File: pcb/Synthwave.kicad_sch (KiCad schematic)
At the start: 61 parts, among them J1 Conn_01x01_Pin, J2 Conn_01x01_Pin, P1 MINI-360, P2 MINI-360, Q1 TIP120, Q10 TIP120, Q2 TIP120, Q3 TIP120, Q4 TIP120, Q5 TIP120, Q6 TIP120, Q7 TIP120, Q8 TIP120, Q9 TIP120, U1 Heltec_HTIT-WB32, U2 L9110

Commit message: Many small updates
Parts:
- added J3: ADC1, Connector_PinSocket_2.54mm:PinSocket_1x03_P2.54mm_Vertical, symbol Connector:Conn_01x03_Socket
- added J4: ADC2, Connector_PinSocket_2.54mm:PinSocket_1x03_P2.54mm_Vertical, symbol Connector:Conn_01x03_Socket
- added J5: ADC3, Connector_PinSocket_2.54mm:PinSocket_1x03_P2.54mm_Vertical, symbol Connector:Conn_01x03_Socket
- added J6: ADC4, Connector_PinSocket_2.54mm:PinSocket_1x03_P2.54mm_Vertical, symbol Connector:Conn_01x03_Socket
- U1: value Heltec_HTIT-WB32 -> Heltec_HTIT-WB32v3
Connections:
- net at R18.1, R8.2: now also U1.2 (34); no longer U1.12
- net at R16.1, R6.2: now also U1.21 (46); no longer U1.17
- net at R14.1, R4.2: now also U1.3 (47); no longer U1.33
- net at R10.2, R20.1: now also U1.19 (42); no longer U1.23
- net at R1.2, R11.1: now also U1.32 (7_ADC); no longer U1.14
- net at U1.1 (48): now also R15.1, R5.2
- net at R17.1, R7.2: now also U1.34 (5_ADC); no longer U1.13
- net at U1.15 (33): now also R13.1, R3.2
- net at U1.18 (40): now also U2.6 (IA)
- net at R19.1, R9.2: now also U1.22 (45); no longer U1.2
- net at P2.3 (OUT+): now also U1.9 (5V), J3.2 (Pin_2), J4.2 (Pin_2), J5.2 (Pin_2), J6.2 (Pin_2); no longer U1.20 (5V)
- net at R12.1, R2.2: now also U1.35 (6_ADC); no longer U1.27
- net at P2.2 (OUT-), U2.5 (GND), U2.8 (GND): now also U1.8 (GND), J3.3 (PIN_3), J4.3 (PIN_3), J5.3 (PIN_3), J6.3 (PIN_3); no longer U1.28 (GND)
- net at U2.7 (IB): now also U1.23 (41); no longer U1.34
- net at U1.36 (VBAT_1_ADC): now also J3.1 (Pin_1)
- net at U1.37 (2_ADC): now also J4.1 (Pin_1)
- net at U1.38 (3_ADC): now also J5.1 (Pin_1)
- net at U1.39 (4_ADC): now also J6.1 (Pin_1)
- now unconnected: U1.25 (25_DAC)
- no-connect marks 23 -> 1
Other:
- moved on the sheet: U1

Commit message: Update and upgrades
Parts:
- added J7, J8: RX, Connector_PinSocket_2.54mm:PinSocket_1x02_P2.54mm_Vertical, symbol Connector:Conn_01x02_Socket
- renumbered DC_OUT1 to PUMP1, DC_OUT2 to PUMP2, DC_OUT9 to REL1, DC_OUT10 to REL2, DC_OUT7 to VAC1, DC_OUT8 to VAC2, DC_OUT3 to VALVE1, DC_OUT4 to VALVE2, DC_OUT5 to VALVE3, DC_OUT6 to VALVE4
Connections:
- net at J3.2 (Pin_2), J4.2 (Pin_2), J5.2 (Pin_2)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: now also J8.2 (Pin_2)
- net at J3.3 (PIN_3), J4.3 (PIN_3), J5.3 (PIN_3)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: now also J8.1 (Pin_1)
- net at U1.12 (43_TX): now also J7.1 (Pin_1)
- net at U1.13 (44_RX): now also J7.2 (Pin_2)
- no-connect marks 1 -> 17
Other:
- note removed: "Pump_1"
- note removed: "Pump_2"
- note removed: "Release_1"
- note removed: "Release_2"
- note removed: "Vacuum_1"
- note removed: "Vacuum_2"
- note removed: "Valve_1"
- note removed: "Valve_2"
- note removed: "Valve_3"
- note removed: "Valve_4"
- moved on the sheet: J6

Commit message: updates
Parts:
- removed J1, J2: Conn_01x01_Pin, Connector_PinSocket_2.54mm:PinSocket_1x01_P2.54mm_Vertical, symbol Connector:Conn_01x01_Pin
- removed P2: MINI-360, Custom Footprints:MINI-360, symbol 74xGxx:MINI-360
- added J1: Barrel_Jack_Switch, Connector_BarrelJack:BarrelJack_Horizontal, symbol Connector:Barrel_Jack_Switch
- added J10: GPIO39, Connector_PinSocket_2.54mm:PinSocket_1x02_P2.54mm_Vertical, symbol Connector:Conn_01x02_Socket
- added J9: GPIO26, Connector_PinSocket_2.54mm:PinSocket_1x02_P2.54mm_Vertical, symbol Connector:Conn_01x02_Socket
- added NT1: NetTie_2, NetTie:NetTie-2_THT_Pad1.0mm, symbol Device:NetTie_2
- added U3: L7805, Package_TO_SOT_THT:TO-220-3_Vertical, symbol Regulator_Linear:L7805
- J7: value RX -> TX
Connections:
- net +15V: now also J1.1, U3.1 (IN)
- net GND: now also U2.5 (GND), U2.8 (GND), J1.2, NT1.2; no longer R11.2, R12.2, R13.2, R14.2, R15.2, R16.2, R17.2, R18.2, R19.2, R20.2
- net +5V: now reaches J3.2 (Pin_2), J4.2 (Pin_2), J5.2 (Pin_2), J6.2 (Pin_2), J8.2 (Pin_2), U1.9 (5V)
- net +5V: now also U3.3 (OUT)
- net GND1: now reaches J3.3 (PIN_3), J4.3 (PIN_3), J5.3 (PIN_3), J6.3 (PIN_3), J8.1 (Pin_1), U1.8 (GND)
- net GND1: now also R11.2, R12.2, R13.2, R14.2, R15.2, R16.2, R17.2, R18.2, R19.2, R20.2, J10.2 (Pin_2), J9.2 (Pin_2), NT1.1, U3.2 (GND); no longer U2.5 (GND), U2.8 (GND)
- net at U1.10 (26): now also J9.1 (Pin_1)
- net at U1.5 (39): now also J10.1 (Pin_1)
- no-connect marks 17 -> 16
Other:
- note added: "ADC breakouts for pH meters"
- note added: "GPIO breakouts for float switches"
- note added: "TX/RX breakouts for CO2 Sensor"
- note removed: "(Set to +5v)"
- moved on the sheet: D1, D10, D2, D3, D4, D5, D6, D7, D8, D9, E2, H1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

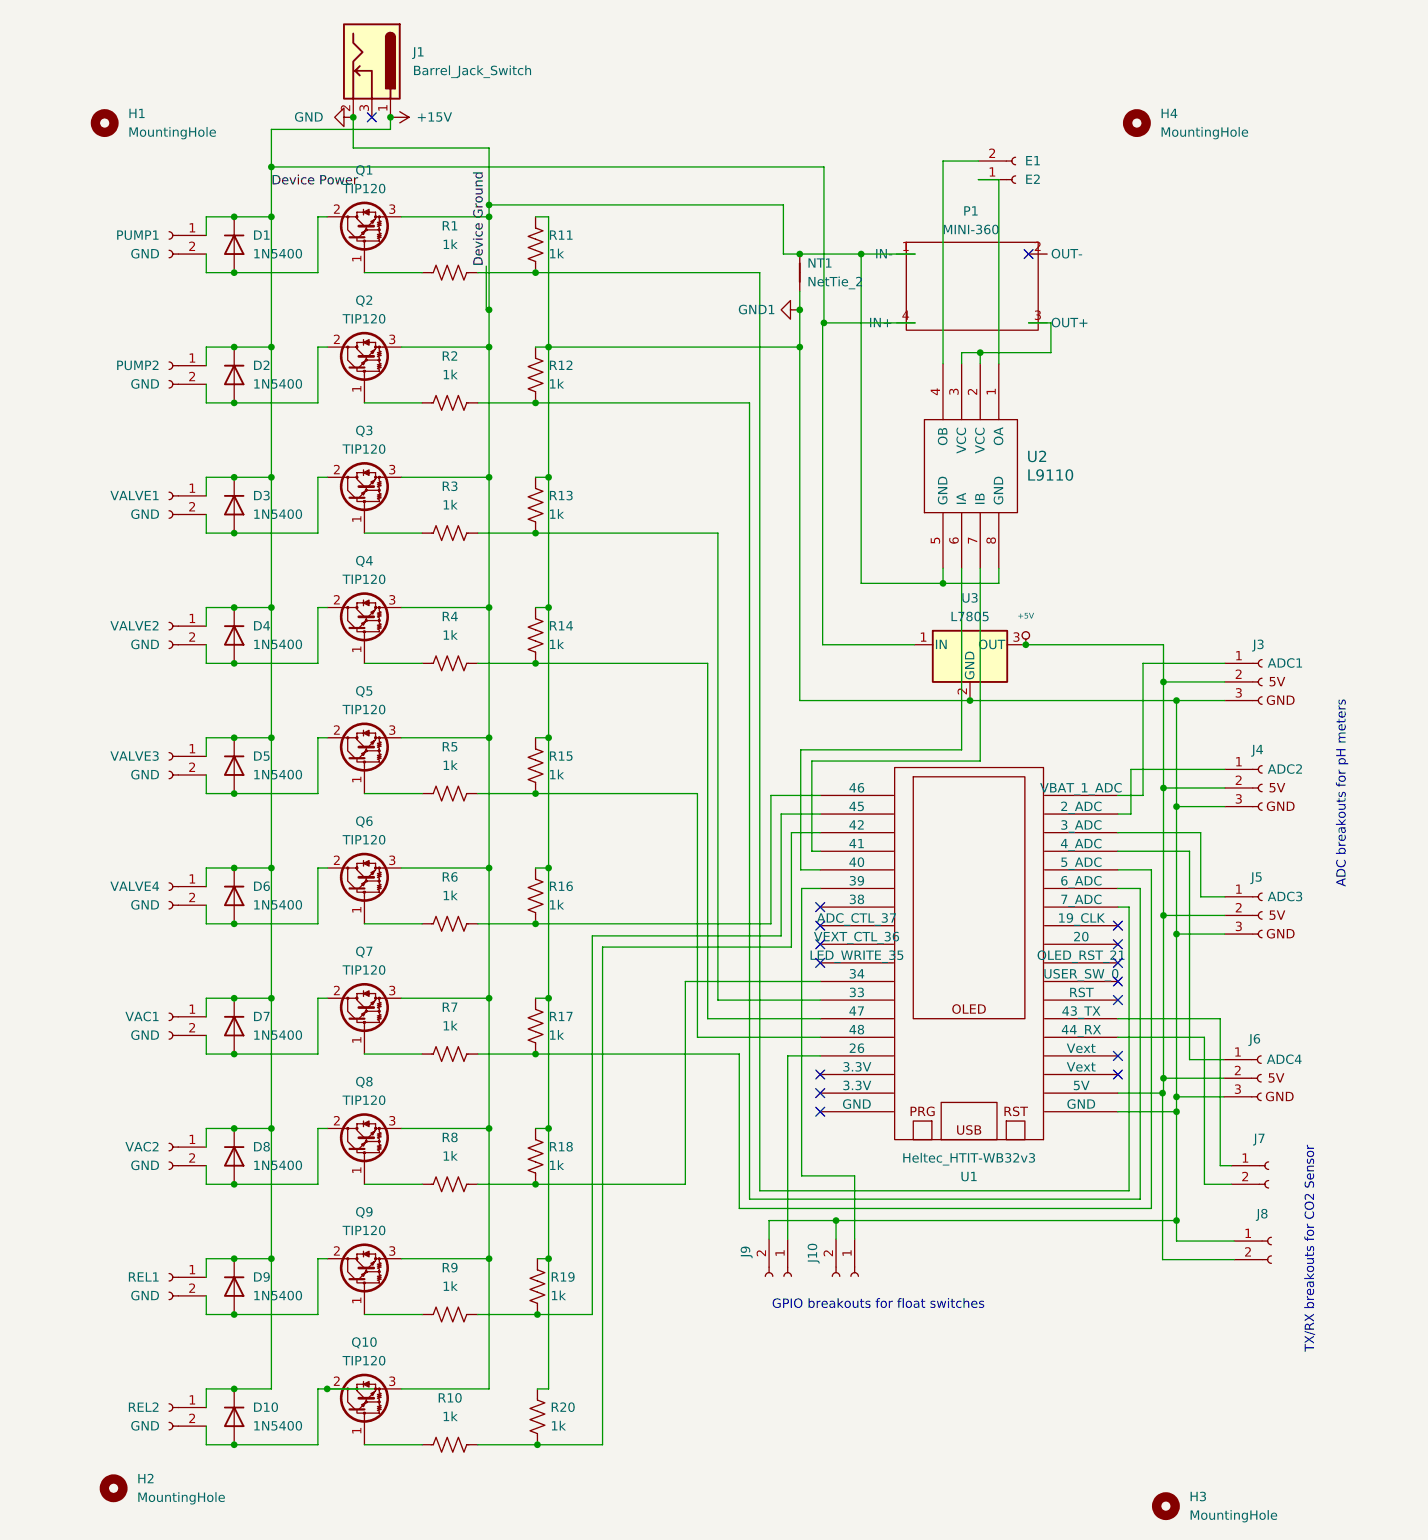
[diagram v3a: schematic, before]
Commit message: Add lots and lots of connectors to PCB
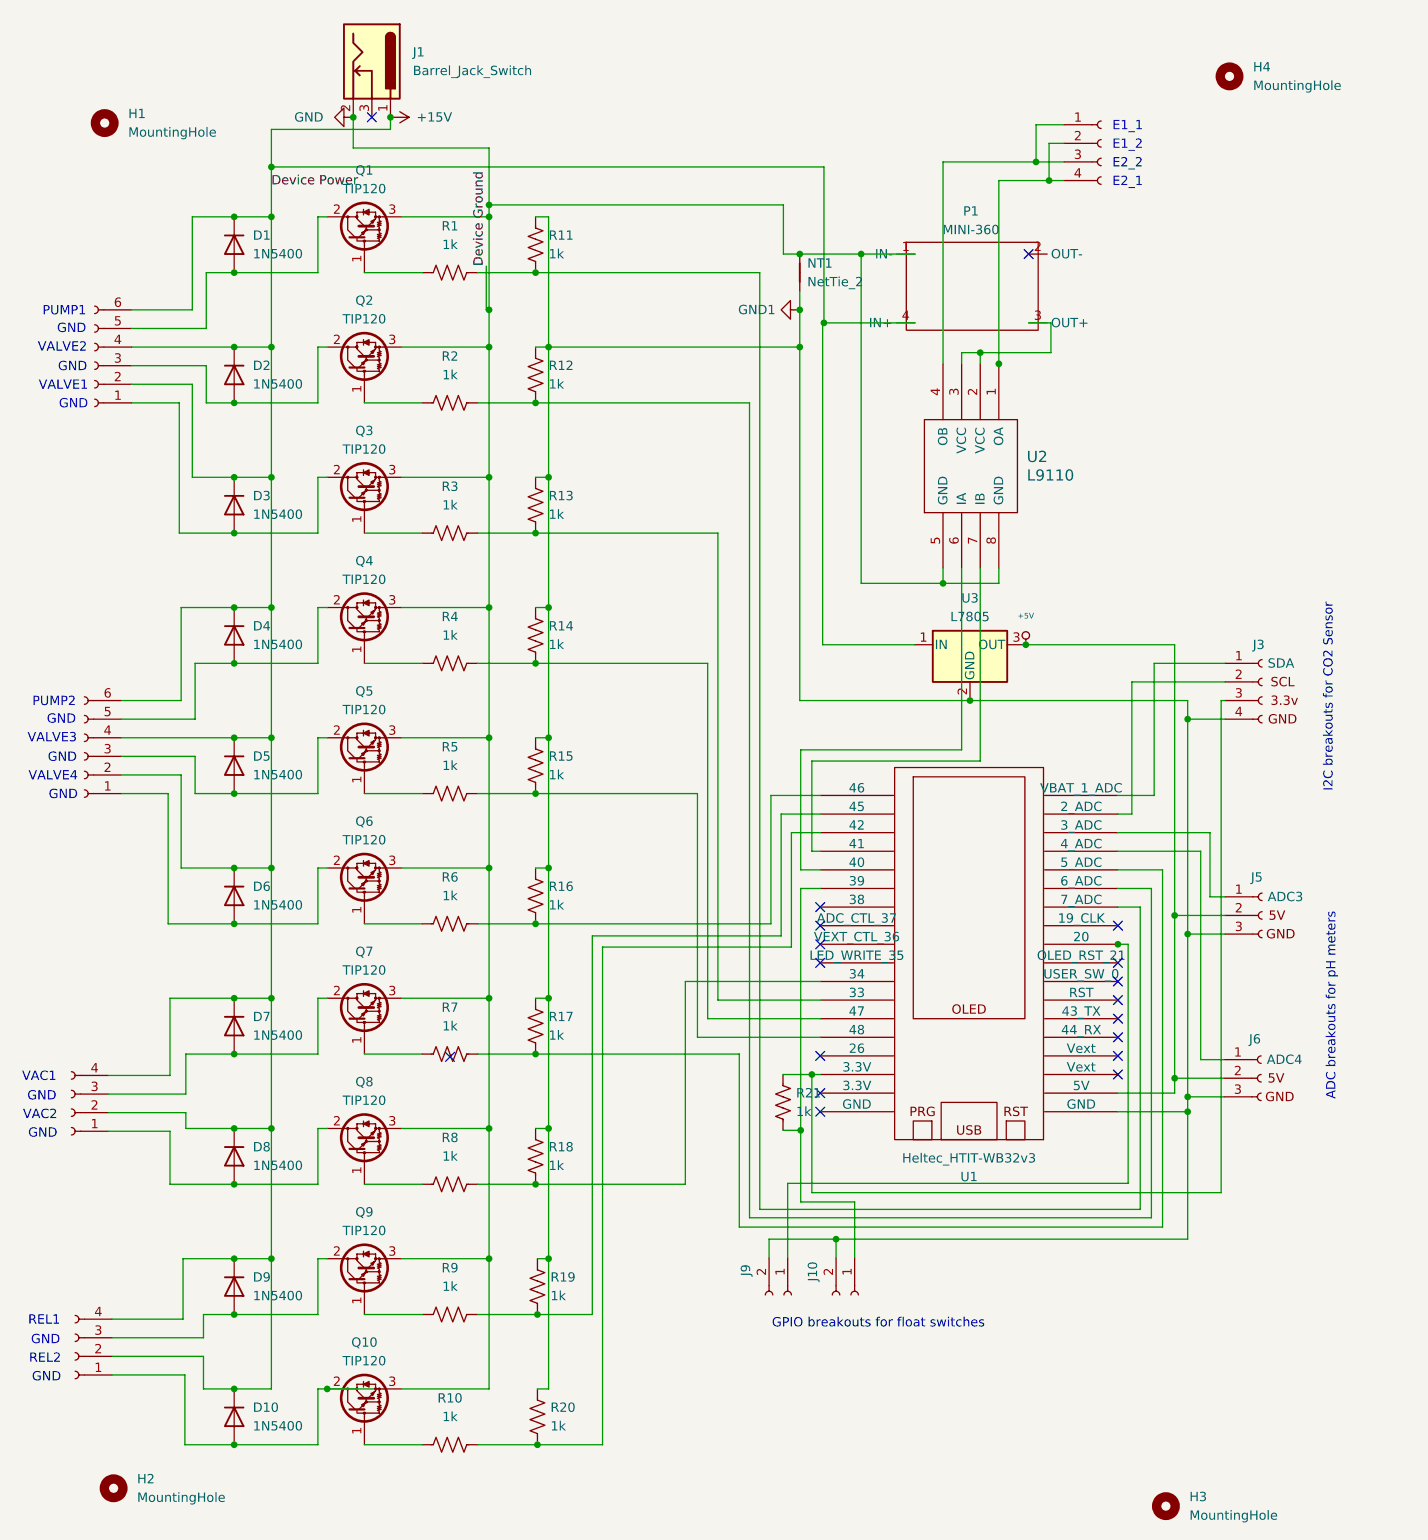
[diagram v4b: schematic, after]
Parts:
- removed E2: E1, Connector_PinSocket_2.54mm:PinSocket_1x02_P2.54mm_Vertical, symbol Connector:Conn_01x02_Socket
- removed J4: ADC2, Connector_PinSocket_2.54mm:PinSocket_1x03_P2.54mm_Vertical, symbol Connector:Conn_01x03_Socket
- removed J7: TX, Connector_PinSocket_2.54mm:PinSocket_1x02_P2.54mm_Vertical, symbol Connector:Conn_01x02_Socket
- removed J8: RX, Connector_PinSocket_2.54mm:PinSocket_1x02_P2.54mm_Vertical, symbol Connector:Conn_01x02_Socket
- removed PUMP1, PUMP2, REL1, REL2, VAC1, VAC2, VALVE1, VALVE2, VALVE3, VALVE4: GND, Connector_PinSocket_2.54mm:PinSocket_1x02_P2.54mm_Vertical, symbol Connector:Conn_01x02_Socket
- added J11, J7, J8: Conn_01x04_Socket, Connector_JST:JST_XH_S4B-XH-A_1x04_P2.50mm_Horizontal, symbol Connector:Conn_01x04_Socket
- added J2, J4: Conn_01x06_Socket, Connector_JST:JST_XH_S6B-XH-A_1x06_P2.50mm_Horizontal, symbol Connector:Conn_01x06_Socket
- added R21: 1k, Resistor_THT:R_Axial_DIN0207_L6.3mm_D2.5mm_P7.62mm_Horizontal, symbol Device:R_US
- J10, J9: footprint Connector_PinSocket_2.54mm:PinSocket_1x02_P2.54mm_Vertical -> Connector_JST:JST_XH_S2B-XH-A_1x02_P2.50mm_Horizontal
- J3: value ADC1 -> SDA; footprint Connector_PinSocket_2.54mm:PinSocket_1x03_P2.54mm_Vertical -> Connector_JST:JST_XH_S4B-XH-A_1x04_P2.50mm_Horizontal; symbol Connector:Conn_01x03_Socket -> Connector:Conn_01x04_Socket
- J5, J6: footprint Connector_PinSocket_2.54mm:PinSocket_1x03_P2.54mm_Vertical -> Connector_JST:JST_PH_S3B-PH-K_1x03_P2.00mm_Horizontal
- NT1: footprint NetTie:NetTie-2_THT_Pad1.0mm -> Connector_PinHeader_2.54mm:PinHeader_1x02_P2.54mm_Vertical
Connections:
- net +15V: now also J2.2 (Pin_2), J2.4 (Pin_4), J2.6 (Pin_6), J4.2 (Pin_2), J4.4 (Pin_4), J4.6 (Pin_6), J7.2 (Pin_2), J7.4 (Pin_4), J8.2 (Pin_2), J8.4 (Pin_4)
- net +5V: no longer J3.2 (Pin_2)
- net GND1: now also J3.4 (Pin_4); no longer J3.3 (PIN_3)
- net at D7.2 (A), Q7.2 (C): now also J7.3 (Pin_3)
- net at U1.37 (2_ADC): now also J3.2 (Pin_2)
- net at D2.2 (A), Q2.2 (C): now also J2.3 (Pin_3)
- net at D3.2 (A), Q3.2 (C): now also J2.1 (Pin_1)
- net at D8.2 (A), Q8.2 (C): now also J7.1 (Pin_1)
- net at J10.1 (Pin_1), U1.5 (39): now also R21.1
- net at D6.2 (A), Q6.2 (C): now also J4.1 (Pin_1)
- net at D10.2 (A), Q10.2 (C): now also J8.1 (Pin_1)
- net at D9.2 (A), Q9.2 (C): now also J8.3 (Pin_3)
- net at D4.2 (A), Q4.2 (C): now also J4.5 (Pin_5)
- net at J9.1 (Pin_1): now also U1.25 (20); no longer U1.10 (26)
- net at U1.11 (3.3V): now also J3.3 (Pin_3), R21.2
- net at D5.2 (A), Q5.2 (C): now also J4.3 (Pin_3)
- net at D1.2 (A), Q1.2 (C): now also J2.5 (Pin_5)
- net at U2.1 (OA): now also J11.2 (Pin_2), J11.4 (Pin_4)
- net at U2.4 (OB): now also J11.1 (Pin_1), J11.3 (Pin_3)
- no-connect marks 16 -> 18
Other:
- note added: "E1_1"
- note added: "E1_2"
- note added: "E2_1"
- note added: "E2_2"
- note added: "GND"
- note added: "I2C breakouts for CO2 Sensor"
- note added: "PUMP1"
- note added: "PUMP2"
- note added: "REL1"
- note added: "REL2"
- note added: "VAC1"
- note added: "VAC2"
- note added: "VALVE1"
- note added: "VALVE2"
- note added: "VALVE3"
- note added: "VALVE4"
- note removed: "TX/RX breakouts for CO2 Sensor"
- moved on the sheet: H4, J10, J9

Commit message: Switch to better buck converter board
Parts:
- removed P1: MINI-360, Custom Footprints:MINI-360, symbol 74xGxx:MINI-360
- added J11: XL4015-5A-PS, Custom Footprints:XL4015-5A-PS, symbol 74xGxx:XL4015-5A-PS
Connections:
- net +15V: now also J11.4 (IN+)
- net GND: now also J11.1 (IN-)
- net at U2.2 (VCC), U2.3 (VCC): now also J11.3 (OUT+)
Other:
- note added: "J2"
- note added: "J4"
- note added: "J7"
- note added: "J8"
- moved on the sheet: U2

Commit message: Combine JST connectors
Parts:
- removed J10: GPIO39, Connector_JST:JST_XH_S2B-XH-A_1x02_P2.50mm_Horizontal, symbol Connector:Conn_01x02_Socket
- removed J9: GPIO26, Connector_JST:JST_XH_S2B-XH-A_1x02_P2.50mm_Horizontal, symbol Connector:Conn_01x02_Socket
- added C1: C_Polarized, Capacitor_THT:CP_Radial_D10.0mm_P7.50mm, symbol Device:C_Polarized
- added J12: Conn_01x04_Socket, Connector_JST:JST_XH_S4B-XH-A_1x04_P2.50mm_Horizontal, symbol Connector:Conn_01x04_Socket
- J11: value Conn_01x04_Socket -> ELEC1 FLOAT1
- renumbered J11 to U4
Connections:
- net +15V: now also C1.1
- net GND: now also C1.2
- net GND1: now also J11.4 (Pin_4), J12.4 (Pin_4)
- net at R21.1: now also J3.3 (Pin_3), U1.11 (3.3V); no longer U1.5 (39)
- net at J11.1 (Pin_1), U2.4 (OB): now also J12.1 (Pin_1); no longer J11.3 (Pin_3)
- net at J11.2 (Pin_2), U2.1 (OA): now also J12.2 (Pin_2); no longer J11.4 (Pin_4)
- net at U1.25 (20): now also J11.3 (Pin_3)
- new net: J12.3 (Pin_3), R21.2, U1.5 (39)
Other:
- note added: "FLOAT1"
- note added: "FLOAT2"
- note removed: "GPIO breakouts for float switches"
- moved on the sheet: R21, U4
